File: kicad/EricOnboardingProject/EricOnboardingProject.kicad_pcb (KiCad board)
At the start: 4 copper layers, 50 x 70 mm, 10 parts, among them U1 MC34063AP

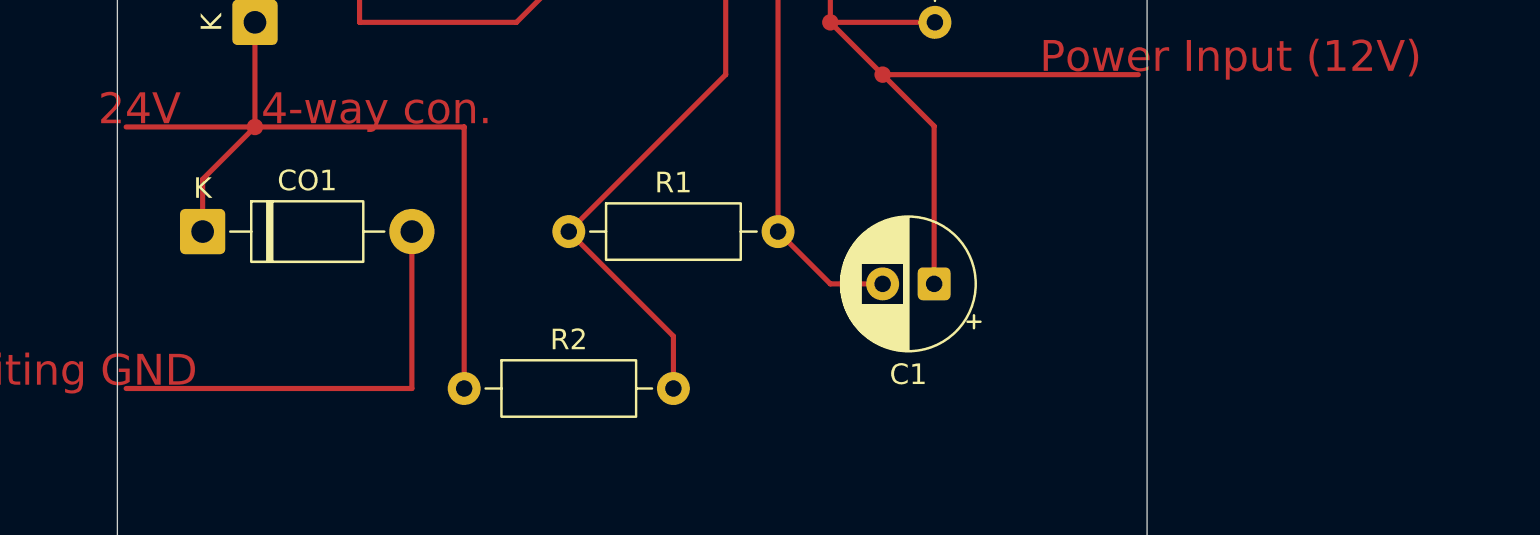
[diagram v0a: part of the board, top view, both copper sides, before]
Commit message: Added a representation of GND leaving circuit
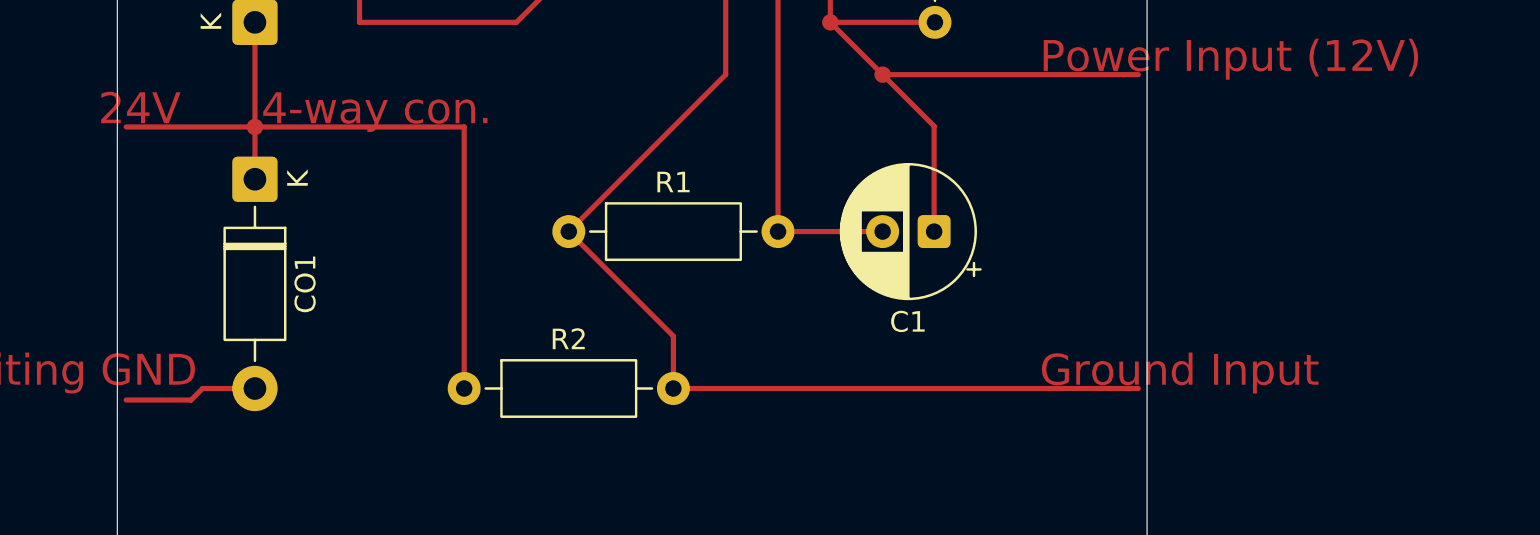
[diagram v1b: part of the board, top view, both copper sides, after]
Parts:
- moved CO1 3.59 mm to (106.7, 127.0), turned to -90 degrees
- moved C1 2.54 mm to (139.7, 129.5)
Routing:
- net Net-(U1-Vfb): track 25.6 -> 48.2 mm
- net GND1: track 21.5 -> 6.49 mm
- net Net-(D1-K): track 40.3 -> 36.7 mm
- net Net-(U1-Vin): track 42.4 -> 39.9 mm
- net GND: track 58.4 -> 57.3 mm
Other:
- board text added: "Ground Input"

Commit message: Edited KiCad to contain actual materials
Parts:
- CT1: value 1500pf -> 680pf
- R1: value 82Ω -> 100+10+10Ω
- R2: value 1500Ω -> 2200Ω
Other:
- board text added: "100uf"
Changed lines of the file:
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@@
 		(tags "CP Radial series Radial pin pitch 2.50mm diameter 6.3mm height 7mm Electrolytic Capacitor")
 		(property "Reference" "C1"
-			(at 1.25 -4.4 0)
+			(at -0.04 -2.54 0)
 			(layer "F.SilkS")
 			(effects
@@
 			)
 		)
-		(property "Value" "1500pf"
+		(property "Value" "680pf"
 			(at 2.5 2.5 90)
 			(layer "F.Fab")
@@
 			)
 		)
-		(property "Value" "82Ω"
+		(property "Value" "100+10+10Ω"
 			(at 5.08 2.37 0)
 			(layer "F.Fab")
@@
 			)
 		)
-		(property "Value" "1500Ω"
+		(property "Value" "2200Ω"
 			(at 5.08 2.37 0)
 			(layer "F.Fab")
@@
 			)
 		)
+	)
+	(gr_text "100uf"
+		(at 139.7 134.62 0)
+		(layer "F.Fab")
+		(effects
+			(font
+				(size 1 1)
+				(thickness 0.15)
+			)
+		)

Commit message: Final edits - solder today
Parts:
- moved CO1 5.08 mm to (106.7, 132.1)
- renumbered D1 to <<D1
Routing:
- net GND: track 57.3 -> 81.9 mm
- net Net-(U1-Vfb): track 48.2 -> 25.6 mm
- net Net-(D1-K): track 36.7 -> 41.8 mm
